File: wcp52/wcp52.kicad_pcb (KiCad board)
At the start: 4 copper layers, 100 x 100 mm, 340 parts, among them J1 MicroUSB-B, J2 IN1, J3 IN2, J4 OUT, J5 9V 300mA, J6 JLINK, J7 AUX, J8 AVR-ICSP, Q1 MMBT3906, Q10 MMBT3904, Q11 BFR540, Q12 BFR540, Q13 MMBT3904, Q14 MMBT3904, Q15 MMBT3904, Q16 MMBT3904, Q17 PZT2907A, Q18 PZT2907A, Q19 MMBT3904, Q2 IRLML6402, Q20 IRLML6402, Q3 AOD417, Q4 MMBT3906, Q5 2N7002, Q6 2N7002, Q7 MMBT3906, Q8 2N7002, Q9 2N7002, U1 TL431AIDBZ, U10 MASWSS0162, U11 AD8310ARMZ, U12 ATSAM4S16CA-AU, U13 FT230XS_DNP, U14 L78M05CDT, U15 MC79M05CDT, U16 AZ1117CH-1.8TRG1, U17 MCP1700T-vv02E/TT, U18 ATMEGA32U4-AU-DNP, U2 LM393M, U3 LMH6714MF, U4 AD9958BCPZ, U5 LMH6714MF, U6 AD8000YRDZ, U7 THS3001IDGN, U8 MAADSS0008, U9 MASWSS0162, X1 25 MHz, X2 12MHz

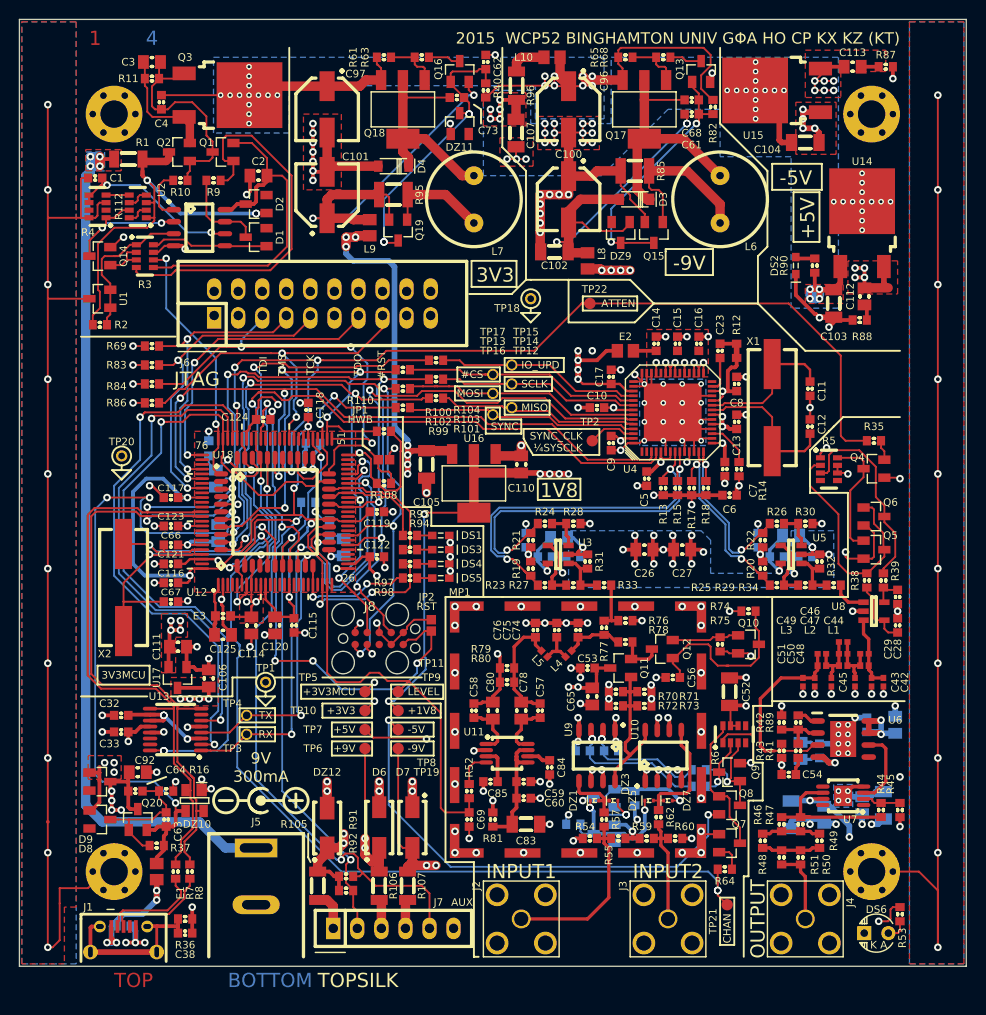
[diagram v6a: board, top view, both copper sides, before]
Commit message: Add power rail diag LEDs
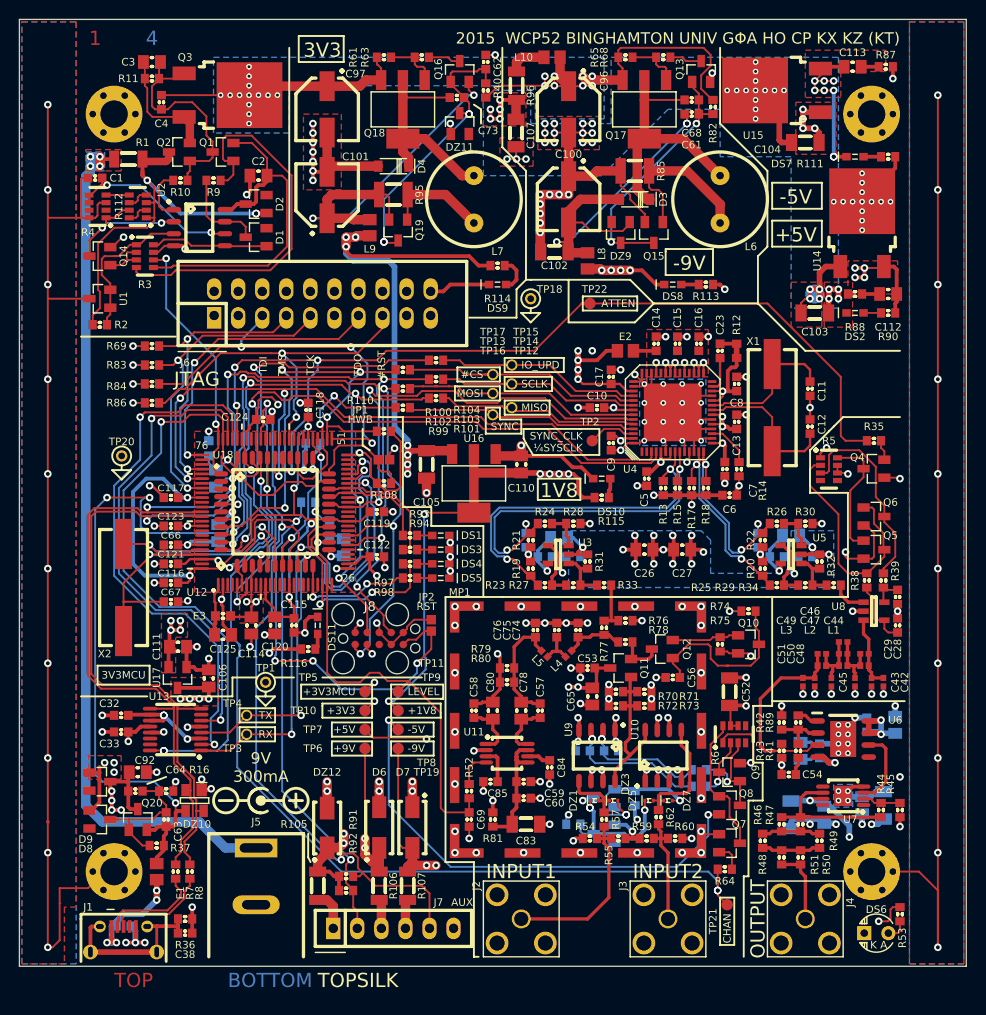
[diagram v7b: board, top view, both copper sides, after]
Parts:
- added DS10: +1V8, smd-semi:LED-0603, F.Cu at (136.5, 73.5)
- added DS11: +3V3MCU, smd-semi:LED-0603, F.Cu at (106.5, 89.0)
- added DS7: -5V, smd-semi:LED-0603, F.Cu at (163.2, 39.5)
- added DS8: -9V, smd-semi:LED-0603, F.Cu at (144.0, 53.0)
- added DS9: +3V3, smd-semi:LED-0603, F.Cu at (125.5, 53.0)
- added R111: 1k6, IPC7351-Nominal:RESC1608X50, F.Cu at (166.8, 39.5)
- added R113: 3k3, IPC7351-Nominal:RESC1608X50, F.Cu at (147.5, 53.0)
- added R114: 1k6, IPC7351-Nominal:RESC1608X50, F.Cu at (125.5, 51.0)
- added R115: 1k6, IPC7351-Nominal:RESC1608X50, F.Cu at (136.5, 75.5)
- added R116: 1k6, IPC7351-Nominal:RESC1608X50, F.Cu at (105.5, 91.5)
- DS2: value PWR -> +5V
- R90: value 3k3 -> 1k6
- moved R90 9.22 mm to (166.8, 56.0), turned to 180 degrees
- moved DS2 8.00 mm to (163.2, 56.0), turned to 0 degrees
- moved R88 2.80 mm to (163.2, 54.0)
- moved C112 2.51 mm to (166.8, 54.0), turned to 180 degrees
- moved C103 2.24 mm to (159.0, 56.0), turned to 0 degrees
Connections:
- R90 pad 1: +9 -> +5
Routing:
- net GND: track 668.4 -> 687.6 mm, vias 254 -> 257
- net +3.3: track 58.1 -> 74.5 mm
- net -5: track 108.7 -> 117.1 mm, vias 23 -> 25
- net +1.8: track 62.3 -> 66.9 mm
- net -9: track 248.7 -> 252.9 mm
- net Net-(DS9-Pad2): track 0.00 -> 3.77 mm
- net +3.3SB: track 70.2 -> 73.7 mm, vias 20 -> 21
- net +5: track 234.2 -> 236.4 mm
- net Net-(DS10-Pad2): track 0.00 -> 2.06 mm
- net Net-(DS8-Pad2): track 0.00 -> 1.85 mm
- net Net-(DS7-Pad2): track 0.00 -> 1.85 mm
- net Net-(DS11-Pad2): track 0.00 -> 1.70 mm
- net /MPU/ATTEN: track 104.1 -> 102.8 mm
- removed copper zone on F.Cu, net /DCDC/IN

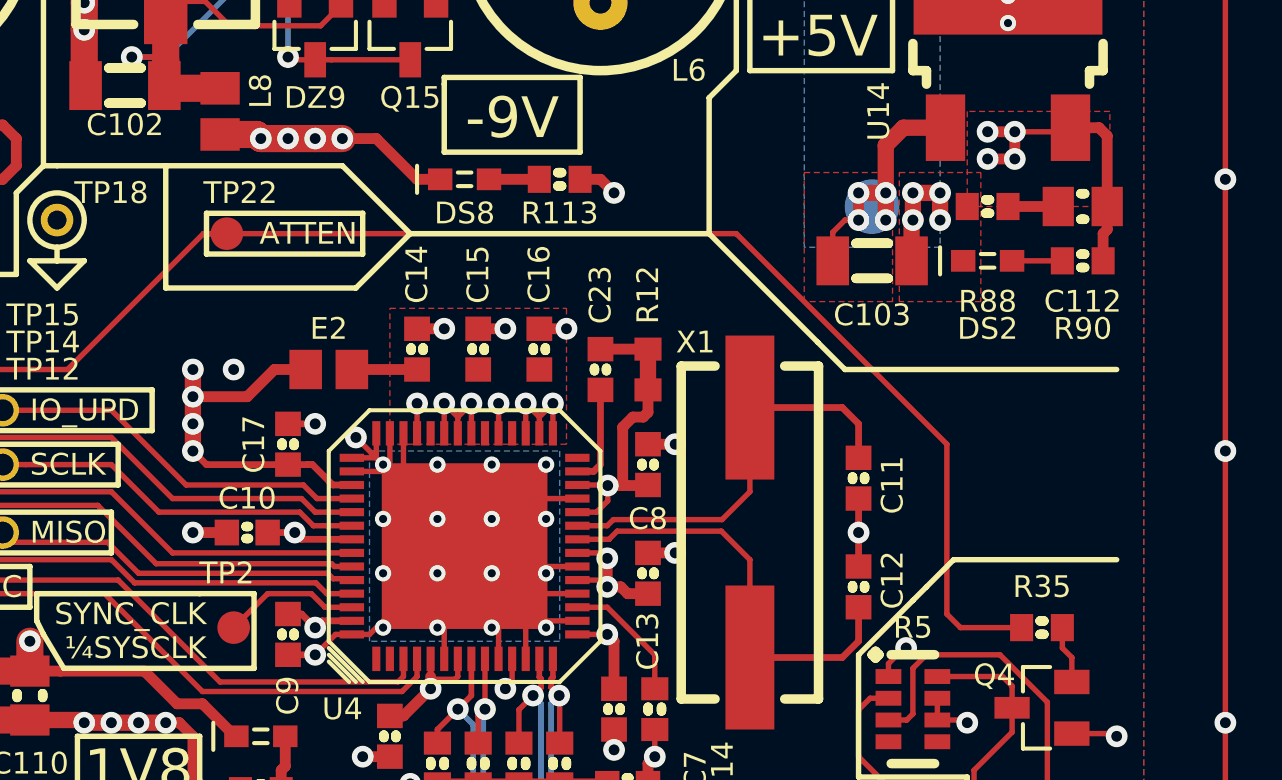
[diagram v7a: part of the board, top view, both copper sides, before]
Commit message: Move ATTEN test point to near attenuator
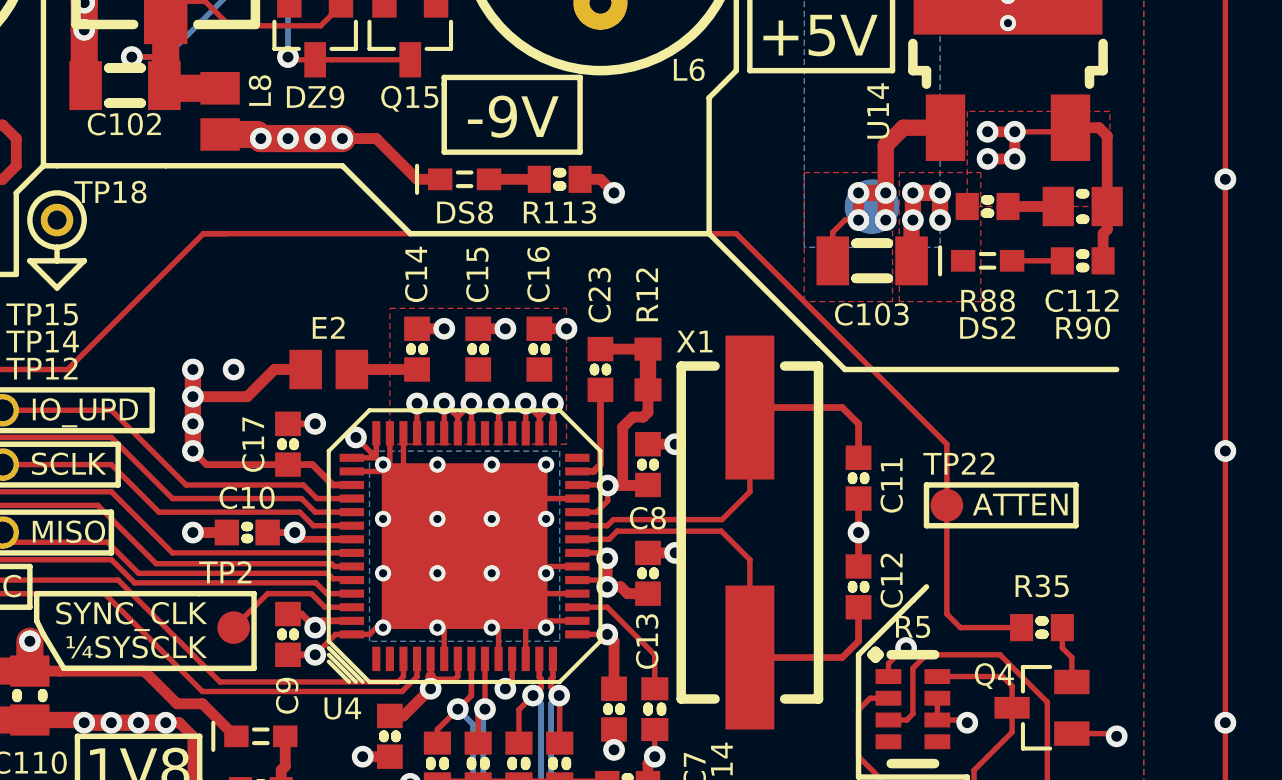
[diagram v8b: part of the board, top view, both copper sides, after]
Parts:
- moved TP22 28.3 mm to (161.8, 65.0)
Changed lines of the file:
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@@
     (links 828)
     (no_connects 0)
-    (area 74.949999 24.949999 175.050001 125.050001)
+    (area 69.899999 19.899999 188.714286 137.4)
     (thickness 1.6)
-    (drawings 677)
-    (tracks 3768)
+    (drawings 672)
+    (tracks 3769)
     (zones 0)
     (modules 350)
@@
   )
   (setup
-    (last_trace_width 0.4)
+    (last_trace_width 0.2)
     (trace_clearance 0.152)
     (zone_clearance 0.2)
@@
   )
   (module conn-test:TEST-SMD-SMALL (layer F.Cu)
-    (at 135.25 55)
+    (at 161.75 65)
     (fp_text reference TP22 (at 0.5 -1.5) (layer F.SilkS)
       (effects (font (size 0.8 0.8) (thickness 0.15)))
@@
     )
   )
+  (gr_line (start 161 65.75) (end 161 64.25) (layer F.SilkS) (width 0.2))
+  (gr_line (start 166.5 65.75) (end 161 65.75) (layer F.SilkS) (width 0.2))
+  (gr_line (start 166.5 64.25) (end 166.5 65.75) (layer F.SilkS) (width 0.2))
+  (gr_line (start 161 64.25) (end 166.5 64.25) (layer F.SilkS) (width 0.2))
   (gr_line (start 127.5 56.5) (end 122.5 56.5) (layer F.SilkS) (width 0.2))
   (gr_line (start 127.5 53.5) (end 127.5 56.5) (layer F.SilkS) (width 0.2))
@@
   (gr_line (start 118.5 78.5) (end 118.5 76.5) (angle 90) (layer F.SilkS) (width 0.2))
   (gr_line (start 124 78.5) (end 118.5 78.5) (angle 90) (layer F.SilkS) (width 0.2))
-  (gr_line (start 133 52.5) (end 133 57) (angle 90) (layer F.SilkS) (width 0.2))
   (gr_line (start 129 52.5) (end 133 52.5) (angle 90) (layer F.SilkS) (width 0.2))
   (gr_line (start 81.5 58.5) (end 91.5 58.5) (angle 90) (layer F.SilkS) (width 0.2))
@@
   (gr_line (start 124 86) (end 124 78.5) (angle 90) (layer F.SilkS) (width 0.2))
   (gr_line (start 126 86) (end 124 86) (angle 90) (layer F.SilkS) (width 0.2))
-  (gr_line (start 162 67) (end 168 67) (angle 90) (layer F.SilkS) (width 0.2))
-  (gr_line (start 161 68) (end 162 67) (angle 90) (layer F.SilkS) (width 0.2))
   (gr_line (start 160.5 68.5) (end 161 68) (angle 90) (layer F.SilkS) (width 0.2))
   (gr_line (start 158.5 70.5) (end 160.5 68.5) (angle 90) (layer F.SilkS) (width 0.2))
@@
   (gr_line (start 153 55) (end 157 59) (angle 90) (layer F.SilkS) (width 0.2))
   (gr_line (start 142 55) (end 153 55) (angle 90) (layer F.SilkS) (width 0.2))
-  (gr_line (start 140 57) (end 142 55) (angle 90) (layer F.SilkS) (width 0.2))
-  (gr_line (start 133 57) (end 140 57) (angle 90) (layer F.SilkS) (width 0.2))
   (gr_line (start 98.25 101.25) (end 98.25 99.75) (layer F.SilkS) (width 0.2))
   (gr_line (start 102 101.25) (end 98.25 101.25) (layer F.SilkS) (width 0.2))
@@
     (effects (font (size 0.8 0.8) (thickness 0.15)))
   )
-  (gr_line (start 134.5 55.75) (end 134.5 54.25) (layer F.SilkS) (width 0.2))
-  (gr_line (start 140.25 55.75) (end 134.5 55.75) (layer F.SilkS) (width 0.2))
-  (gr_line (start 140.25 54.25) (end 140.25 55.75) (layer F.SilkS) (width 0.2))
-  (gr_line (start 134.5 54.25) (end 140.25 54.25) (layer F.SilkS) (width 0.2))
-  (gr_text ATTEN (at 138.25 55) (layer F.SilkS)
+  (gr_text ATTEN (at 164.5 65) (layer F.SilkS)
     (effects (font (size 0.8 0.8) (thickness 0.15)))
   )
@@
   (segment (start 115.77 121) (end 115.77 118.23) (width 1) (layer F.Cu) (net 170))
   (segment (start 115.77 118.23) (end 116 118) (width 1) (layer F.Cu) (net 170))
+  (segment (start 161.75 65) (end 161.75 69) (width 0.2) (layer F.Cu) (net 171))
+  (segment (start 161.75 62.75) (end 161.75 65) (width 0.2) (layer F.Cu) (net 171))
   (segment (start 134.386326 55) (end 154 55) (width 0.2) (layer F.Cu) (net 171))
   (segment (start 154 55) (end 161.75 62.75) (width 0.2) (layer F.Cu) (net 171))
-  (segment (start 161.75 62.75) (end 161.75 69) (width 0.2) (layer F.Cu) (net 171))
   (segment (start 161.75 69) (end 162.25 69.5) (width 0.2) (layer F.Cu) (net 171))
   (segment (start 162.25 69.5) (end 164.5 69.5) (width 0.2) (layer F.Cu) (net 171))
